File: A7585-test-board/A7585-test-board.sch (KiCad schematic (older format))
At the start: 25 parts, among them J100 Conn_Coaxial_Power, SW201 SW_SPDT, SW302 SW_Push_SPDT, SW303 SW_Push_SPDT, U100 MPM3610, U200 A7585D, U300 Pico

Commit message: Minor schematic changes. Layout V1
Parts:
- added H1, H2, H3, H4: MountingHole, MountingHole:MountingHole_3.2mm_M3, symbol Mechanical:MountingHole
- added J2, J3: Conn_01x20, Connector_PinHeader_2.54mm:PinHeader_1x20_P2.54mm_Vertical, symbol Connector_Generic:Conn_01x20
- added J4: Conn_Coaxial_Power, Connector:Banana_Jack_1Pin, symbol Connector:Conn_Coaxial_Power
- C202, C204: footprint (none) -> Capacitor_SMD:C_1206_3216Metric
- D101, D201, D202, D300, D301: footprint (none) -> LED_THT:LED_D4.0mm
- J1: renamed from J?; footprint (none) -> A7585-test-board:Connector_Strip
- J100: footprint (none) -> Connector_BarrelJack:BarrelJack_Horizontal
- JP201, JP202, JP3: footprint (none) -> Connector_PinHeader_2.54mm:PinHeader_1x02_P2.54mm_Vertical
- R101, R201, R202, R203, R204, R301: footprint (none) -> Resistor_SMD:R_1206_3216Metric
- RV301: footprint (none) -> A7585-test-board:Potentiometer_Piher_T-16H_Single_Horizontal
- SW201: footprint (none) -> A7585-test-board:SW_DIP_SPSTx01_Slide_9.78x4.72mm_W7.62mm_P2.54mm
- SW302, SW303: footprint (none) -> A7585-test-board:PUSH_BUTTON
- U100: footprint (none) -> A7585-test-board:MPM3610
- U200: footprint (none) -> A7585-test-board:A7585D_Board
- U300: footprint RPi_Pico:RPi_Pico_SMD_TH -> A7585-test-board:RPi_Pico_SMD_TH
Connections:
- net labels removed: Vdrive

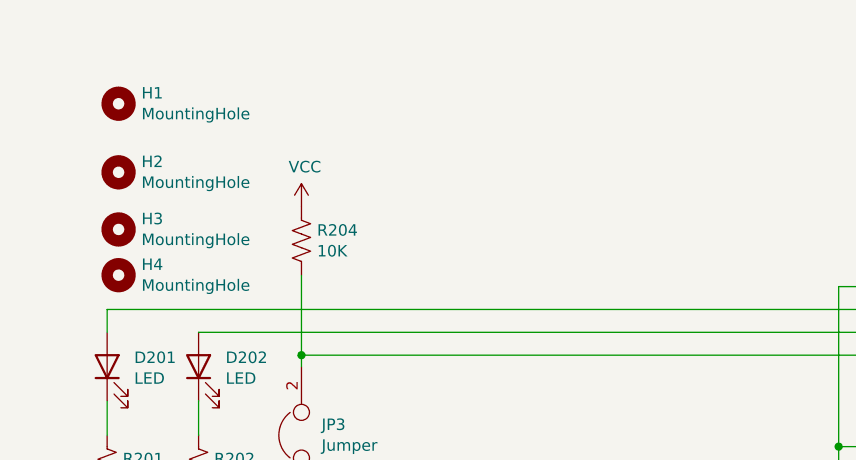
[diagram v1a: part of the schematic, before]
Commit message: Grounded mounting holes. Fixed power plane
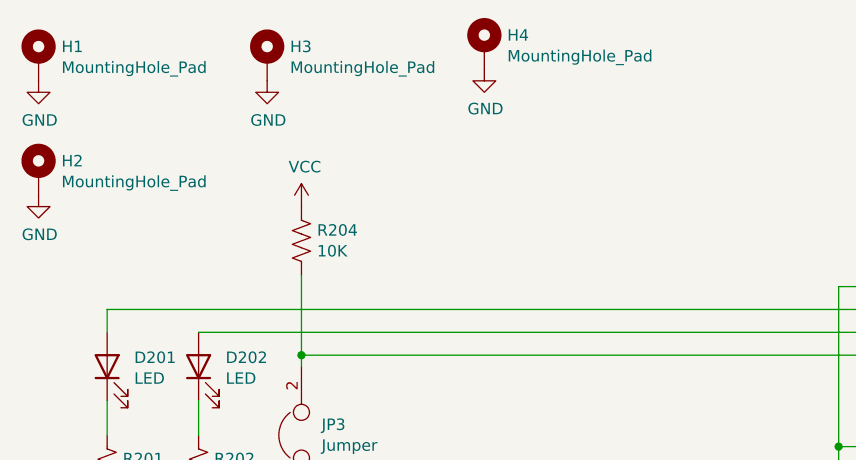
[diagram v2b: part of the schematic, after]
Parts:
- removed H1, H2, H3, H4: MountingHole, MountingHole:MountingHole_3.2mm_M3, symbol Mechanical:MountingHole
- added H1, H2, H3, H4: MountingHole_Pad, MountingHole:MountingHole_3.2mm_M3_Pad, symbol Mechanical:MountingHole_Pad
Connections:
- net GND: now also H1.1, H2.1, H3.1, H4.1
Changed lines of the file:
@@
 	950  1950 950  1850
-$Comp
-L Device:Jumper JP3
-U 1 1 60BA667A
-P 1800 2400
-F 0 "JP3" V 1846 2312 50  0000 R CNN
-F 1 "Jumper" V 1755 2312 50  0000 R CNN
-F 2 "Connector_PinHeader_2.54mm:PinHeader_1x02_P2.54mm_Vertical" H 1800 2400 50  0001 C CNN
-F 3 "~" H 1800 2400 50  0001 C CNN
-	1    1800 2400
-	0    -1   -1   0
-$EndComp
 $Comp
 L Device:R_US R204
@@
 F 3 "~" H 1800 1550 50  0001 C CNN
 	1    1800 1550
-	1    0    0    -1
-$EndComp
-$Comp
-L power:GND #PWR0107
-U 1 1 60BAB54E
-P 1800 2700
-F 0 "#PWR0107" H 1800 2450 50  0001 C CNN
-F 1 "GND" H 1805 2527 50  0000 C CNN
-F 2 "" H 1800 2700 50  0001 C CNN
-F 3 "" H 1800 2700 50  0001 C CNN
-	1    1800 2700
 	1    0    0    -1
 $EndComp
@@
 Text Notes 4250 6150 0    50   ~ 0
 I2C bus 1
-$Comp
-L Mechanical:MountingHole H1
-U 1 1 61100308
-P 1000 950
-F 0 "H1" H 1100 996 50  0000 L CNN
-F 1 "MountingHole" H 1100 905 50  0000 L CNN
-F 2 "MountingHole:MountingHole_3.2mm_M3" H 1000 950 50  0001 C CNN
-F 3 "~" H 1000 950 50  0001 C CNN
-	1    1000 950
-	1    0    0    -1
-$EndComp
-$Comp
-L Mechanical:MountingHole H2
-U 1 1 6110B90D
-P 1000 1250
-F 0 "H2" H 1100 1296 50  0000 L CNN
-F 1 "MountingHole" H 1100 1205 50  0000 L CNN
-F 2 "MountingHole:MountingHole_3.2mm_M3" H 1000 1250 50  0001 C CNN
-F 3 "~" H 1000 1250 50  0001 C CNN
-	1    1000 1250
-	1    0    0    -1
-$EndComp
-$Comp
-L Mechanical:MountingHole H3
-U 1 1 6110BFC1
-P 1000 1500
-F 0 "H3" H 1100 1546 50  0000 L CNN
-F 1 "MountingHole" H 1100 1455 50  0000 L CNN
-F 2 "MountingHole:MountingHole_3.2mm_M3" H 1000 1500 50  0001 C CNN
-F 3 "~" H 1000 1500 50  0001 C CNN
-	1    1000 1500
-	1    0    0    -1
-$EndComp
-$Comp
-L Mechanical:MountingHole H4
-U 1 1 6110C5E9
-P 1000 1700
-F 0 "H4" H 1100 1746 50  0000 L CNN
-F 1 "MountingHole" H 1100 1655 50  0000 L CNN
-F 2 "MountingHole:MountingHole_3.2mm_M3" H 1000 1700 50  0001 C CNN
-F 3 "~" H 1000 1700 50  0001 C CNN
-	1    1000 1700
-	1    0    0    -1
-$EndComp
 Wire Wire Line
 	4150 4850 4600 4850
@@
 	0    -1   1    0
 $EndComp
+$Comp
+L Mechanical:MountingHole_Pad H1
+U 1 1 610A1B28
+P 650 750
+F 0 "H1" H 750 799 50  0000 L CNN
+F 1 "MountingHole_Pad" H 750 708 50  0000 L CNN
+F 2 "MountingHole:MountingHole_3.2mm_M3_Pad" H 650 750 50  0001 C CNN
+F 3 "~" H 650 750 50  0001 C CNN
+	1    650  750
+	1    0    0    -1
+$EndComp
+$Comp
+L Mechanical:MountingHole_Pad H4
+U 1 1 610A2491
+P 2600 700
+F 0 "H4" H 2700 749 50  0000 L CNN
+F 1 "MountingHole_Pad" H 2700 658 50  0000 L CNN
+F 2 "MountingHole:MountingHole_3.2mm_M3_Pad" H 2600 700 50  0001 C CNN
+F 3 "~" H 2600 700 50  0001 C CNN
+	1    2600 700
+	1    0    0    -1
+$EndComp
+$Comp
+L Mechanical:MountingHole_Pad H2
+U 1 1 610A27A1
+P 650 1250
+F 0 "H2" H 750 1299 50  0000 L CNN
+F 1 "MountingHole_Pad" H 750 1208 50  0000 L CNN
+F 2 "MountingHole:MountingHole_3.2mm_M3_Pad" H 650 1250 50  0001 C CNN
+F 3 "~" H 650 1250 50  0001 C CNN
+	1    650  1250
+	1    0    0    -1
+$EndComp
+$Comp
+L Mechanical:MountingHole_Pad H3
+U 1 1 610A333E
+P 1650 750
+F 0 "H3" H 1750 799 50  0000 L CNN
+F 1 "MountingHole_Pad" H 1750 708 50  0000 L CNN
+F 2 "MountingHole:MountingHole_3.2mm_M3_Pad" H 1650 750 50  0001 C CNN
+F 3 "~" H 1650 750 50  0001 C CNN
+	1    1650 750
+	1    0    0    -1
+$EndComp
+$Comp
+L power:GND #PWR0107
+U 1 1 60BAB54E
+P 1800 2700
+F 0 "#PWR0107" H 1800 2450 50  0001 C CNN
+F 1 "GND" H 1805 2527 50  0000 C CNN
+F 2 "" H 1800 2700 50  0001 C CNN
+F 3 "" H 1800 2700 50  0001 C CNN
+	1    1800 2700
+	1    0    0    -1
+$EndComp
+$Comp
+L Device:Jumper JP3
+U 1 1 60BA667A
+P 1800 2400
+F 0 "JP3" V 1846 2312 50  0000 R CNN
+F 1 "Jumper" V 1755 2312 50  0000 R CNN
+F 2 "Connector_PinHeader_2.54mm:PinHeader_1x02_P2.54mm_Vertical" H 1800 2400 50  0001 C CNN
+F 3 "~" H 1800 2400 50  0001 C CNN
+	1    1800 2400
+	0    -1   -1   0
+$EndComp
+$Comp
+L power:GND #PWR03
+U 1 1 610A737A
+P 1650 850
+F 0 "#PWR03" H 1650 600 50  0001 C CNN
+F 1 "GND" H 1655 677 50  0000 C CNN
+F 2 "" H 1650 850 50  0001 C CNN
+F 3 "" H 1650 850 50  0001 C CNN
+	1    1650 850
+	1    0    0    -1
+$EndComp
+$Comp
+L power:GND #PWR04
+U 1 1 610A79D5
+P 2600 800
+F 0 "#PWR04" H 2600 550 50  0001 C CNN
+F 1 "GND" H 2605 627 50  0000 C CNN
+F 2 "" H 2600 800 50  0001 C CNN
+F 3 "" H 2600 800 50  0001 C CNN
+	1    2600 800
+	1    0    0    -1
+$EndComp
+$Comp
+L power:GND #PWR02
+U 1 1 610A7D20
+P 650 1350
+F 0 "#PWR02" H 650 1100 50  0001 C CNN
+F 1 "GND" H 655 1177 50  0000 C CNN
+F 2 "" H 650 1350 50  0001 C CNN
+F 3 "" H 650 1350 50  0001 C CNN
+	1    650  1350
+	1    0    0    -1
+$EndComp
+$Comp
+L power:GND #PWR01
+U 1 1 610A8025
+P 650 850
+F 0 "#PWR01" H 650 600 50  0001 C CNN
+F 1 "GND" H 655 677 50  0000 C CNN
+F 2 "" H 650 850 50  0001 C CNN
+F 3 "" H 650 850 50  0001 C CNN
+	1    650  850
+	1    0    0    -1
+$EndComp
 $EndSCHEMATC

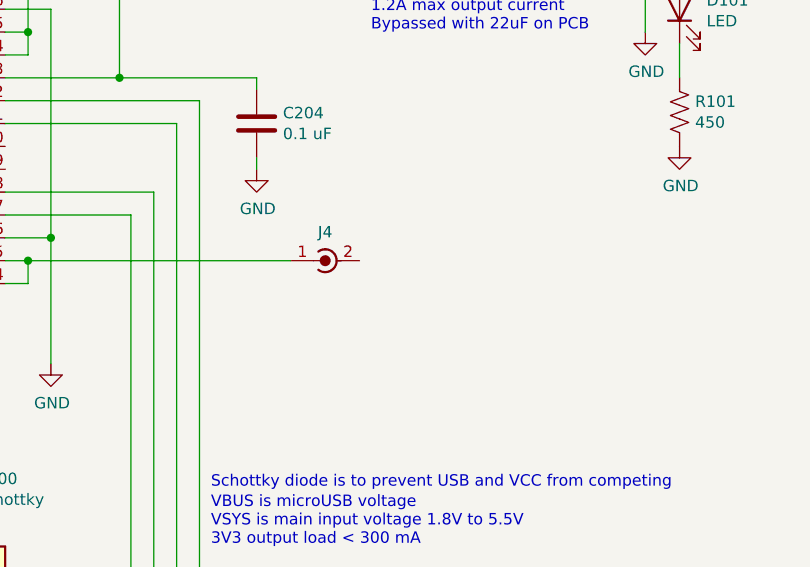
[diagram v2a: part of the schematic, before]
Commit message: New Banana Jacks
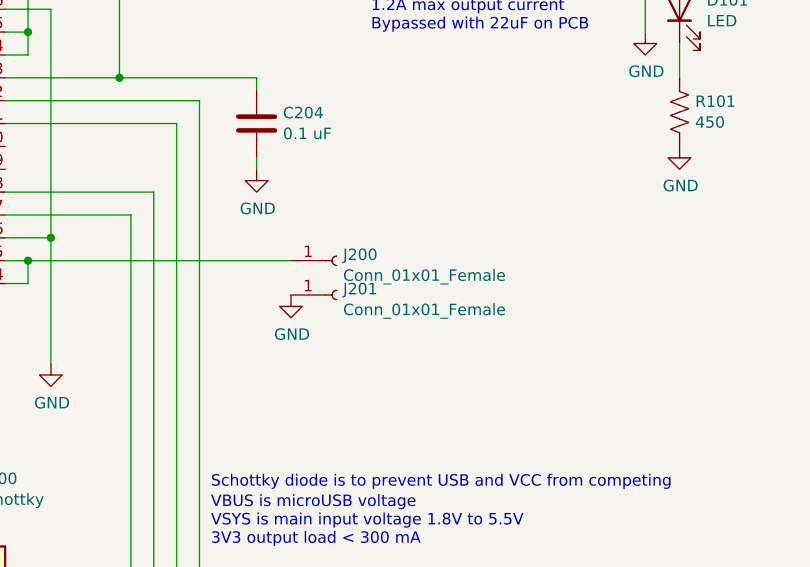
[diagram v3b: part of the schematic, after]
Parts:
- removed J4: Conn_Coaxial_Power, Connector:Banana_Jack_1Pin, symbol Connector:Conn_Coaxial_Power
- added J200, J201: Conn_01x01_Female, A7585-test-board:SMA_Molex_73251-2200_Horizontal, symbol Connector:Conn_01x01_Female
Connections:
- net GND: now also J201.1 (Pin_1)
- net at U200.14 (HV_OUT), U200.15 (HV_OUT): now also J200.1 (Pin_1)
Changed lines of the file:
@@
 	6350 2850 7500 2850
-$Comp
-L Connector:Conn_Coaxial_Power J4
-U 1 1 611FF83A
-P 7600 2850
-F 0 "J4" V 7475 2800 50  0000 C CNN
-F 1 "Conn_Coaxial_Power" H 7688 2755 50  0001 L CNN
-F 2 "Connector:Banana_Jack_1Pin" H 7600 2800 50  0001 C CNN
-F 3 "~" H 7600 2800 50  0001 C CNN
-	1    7600 2850
-	0    -1   1    0
-$EndComp
 $Comp
 L Mechanical:MountingHole_Pad H1
@@
 	1    0    0    -1
 $EndComp
+$Comp
+L power:GND #PWR0113
+U 1 1 610EF2A9
+P 7500 3000
+F 0 "#PWR0113" H 7500 2750 50  0001 C CNN
+F 1 "GND" H 7505 2827 50  0000 C CNN
+F 2 "" H 7500 3000 50  0001 C CNN
+F 3 "" H 7500 3000 50  0001 C CNN
+	1    7500 3000
+	1    0    0    -1
+$EndComp
+$Comp
+L Connector:Conn_01x01_Female J200
+U 1 1 6111CAAF
+P 7700 2850
+F 0 "J200" H 7728 2876 50  0000 L CNN
+F 1 "Conn_01x01_Female" H 7728 2785 50  0000 L CNN
+F 2 "A7585-test-board:SMA_Molex_73251-2200_Horizontal" H 7700 2850 50  0001 C CNN
+F 3 "~" H 7700 2850 50  0001 C CNN
+	1    7700 2850
+	1    0    0    -1
+$EndComp
+$Comp
+L Connector:Conn_01x01_Female J201
+U 1 1 6111D07E
+P 7700 3000
+F 0 "J201" H 7728 3026 50  0000 L CNN
+F 1 "Conn_01x01_Female" H 7728 2935 50  0000 L CNN
+F 2 "A7585-test-board:SMA_Molex_73251-2200_Horizontal" H 7700 3000 50  0001 C CNN
+F 3 "~" H 7700 3000 50  0001 C CNN
+	1    7700 3000
+	1    0    0    -1
+$EndComp

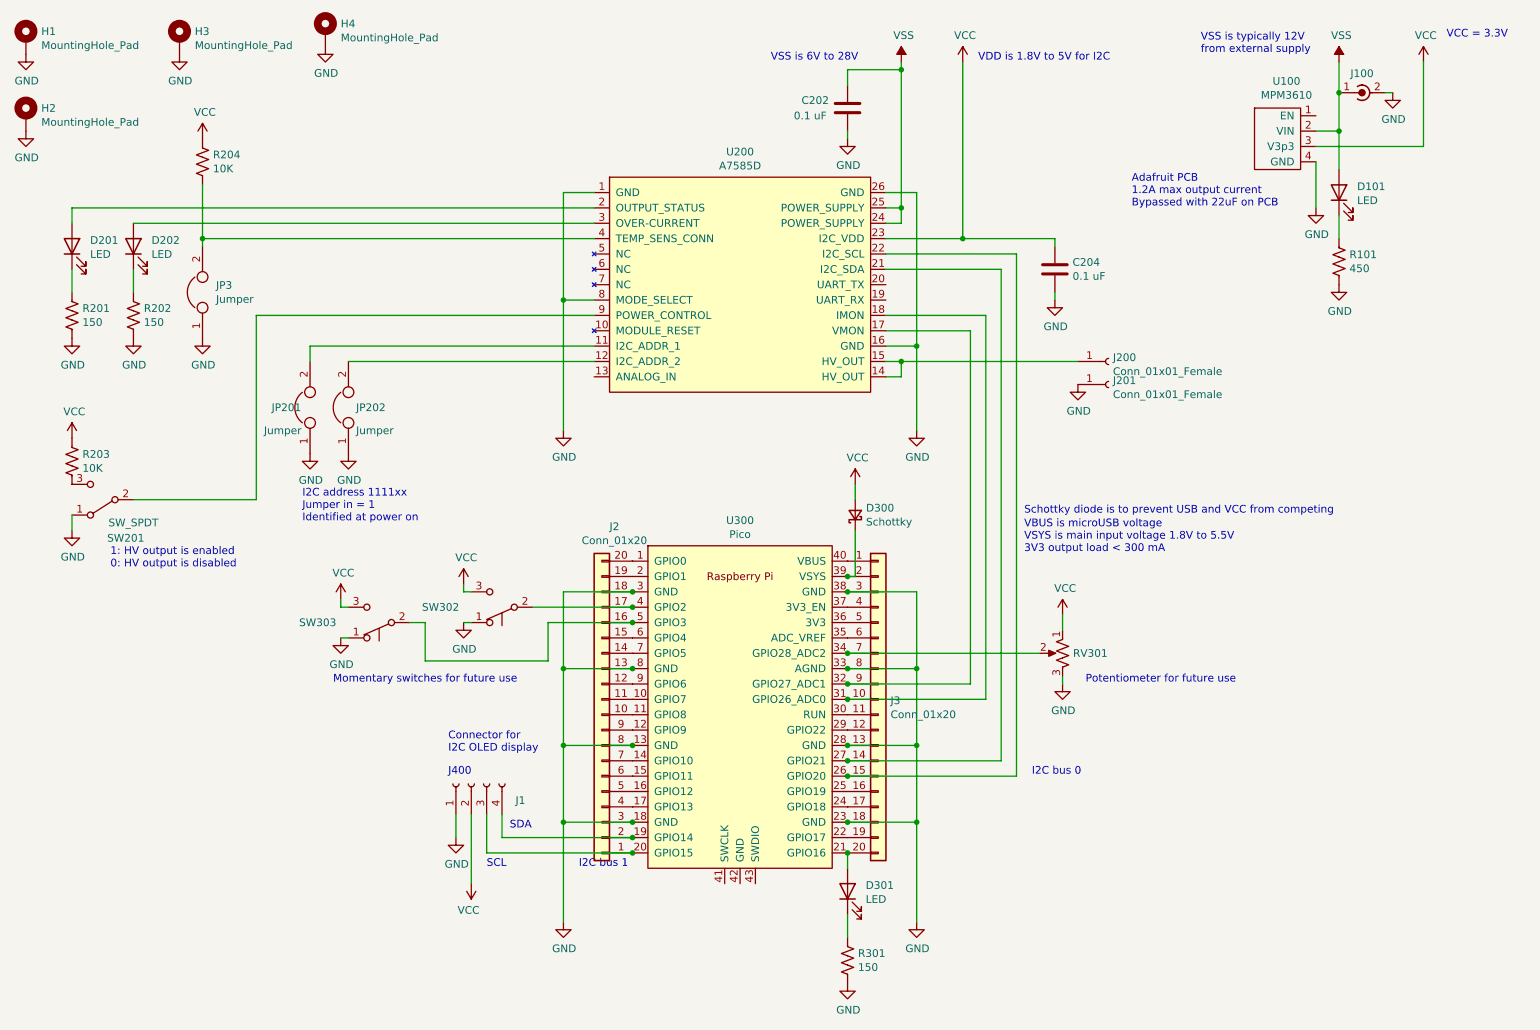
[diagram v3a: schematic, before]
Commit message: New circuit diagram with rotary encoder and precision voltage reference.
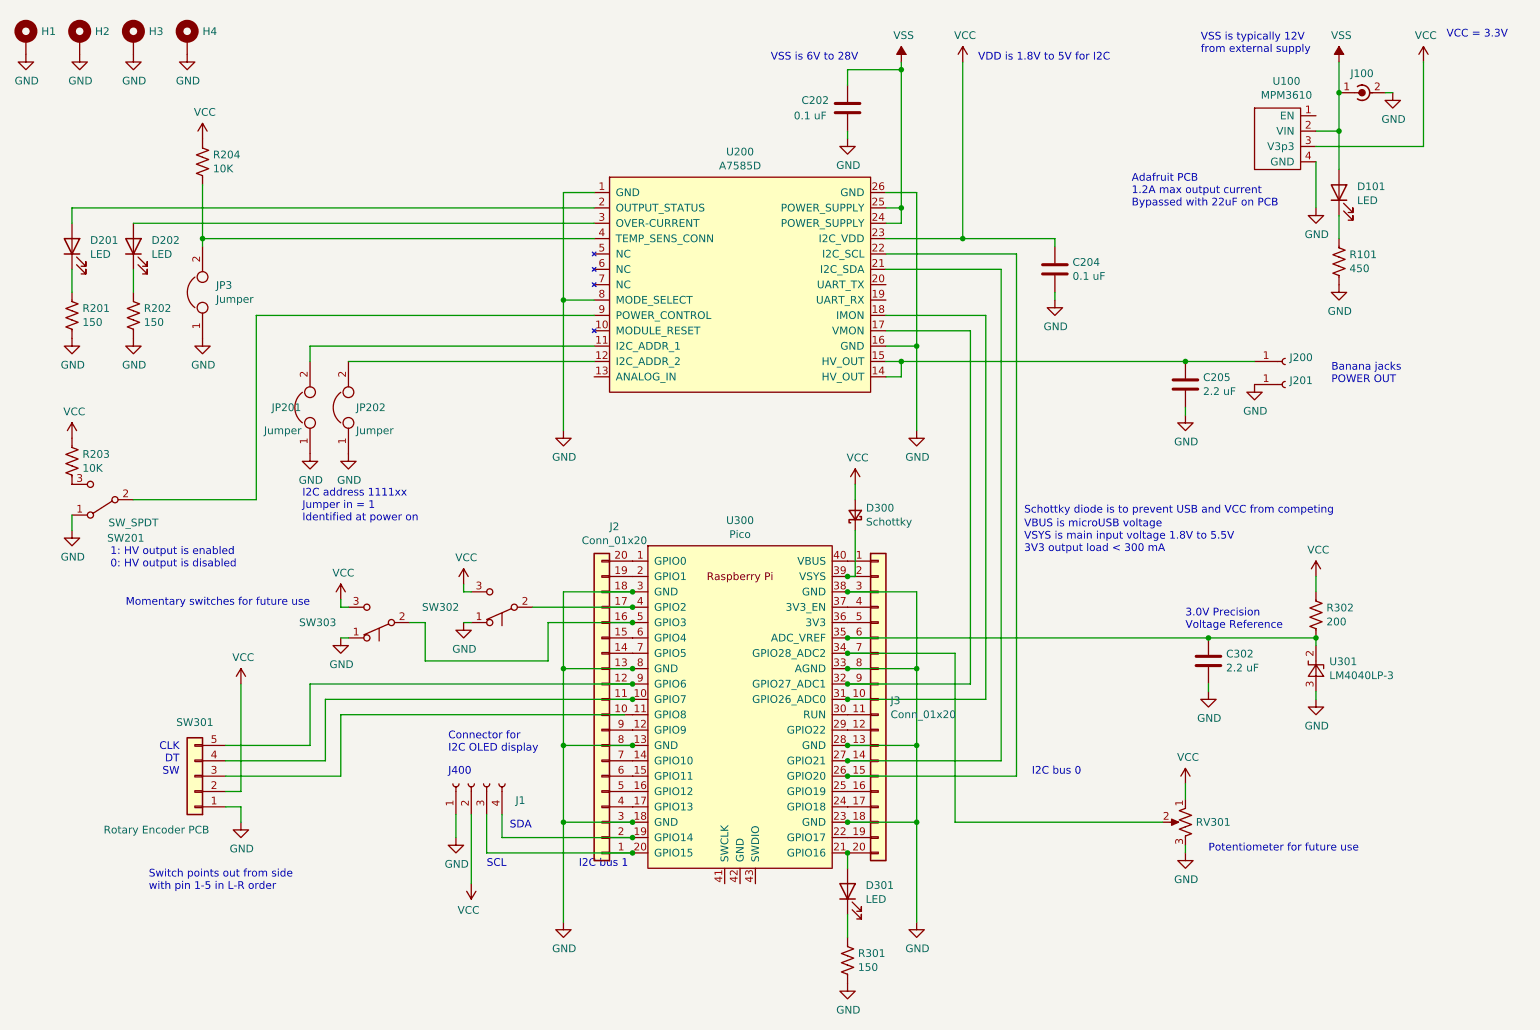
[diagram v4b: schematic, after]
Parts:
- added C205, C302: 2.2 uF, Capacitor_SMD:C_1206_3216Metric, symbol Device:C
- added R302: 200, Resistor_SMD:R_1206_3216Metric, symbol Device:R_US
- added SW301: Rotary Encoder PCB, symbol Connector_Generic:Conn_01x05
- added U301: LM4040LP-3, Package_TO_SOT_THT:TO-92_Inline, symbol Reference_Voltage:LM4040LP-3
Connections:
- net GND: now also C205.2, C302.2, SW301.1 (Pin_1), U301.3 (A)
- net VCC: now also R302.1, SW301.2 (Pin_2)
- net at J200.1 (Pin_1), U200.14 (HV_OUT), U200.15 (HV_OUT): now also C205.1
- net at J2.11 (Pin_11), U300.10 (GPIO7): now also SW301.4 (Pin_4)
- net at J3.6 (Pin_6), U300.35 (ADC_VREF): now also C302.1, R302.2, U301.2 (K)
- net at J2.12 (Pin_12), U300.9 (GPIO6): now also SW301.5 (Pin_5)
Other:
- note added: "3.0V Precision \nVoltage Reference"
- note added: "Banana jacks\nPOWER OUT"
- note added: "CLK\nDT\nSW"
- note added: "Switch points out from side\nwith pin 1-5 in L-R order"
- moved on the sheet: H2, H3, H4, J200, J201, RV301

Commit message: Add files via upload
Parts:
- J200, J201: footprint A7585-test-board:SMA_Molex_73251-2200_Horizontal -> A7585-test-board:Bannana_Jack_2pin
- SW301: footprint (none) -> Connector_PinHeader_2.54mm:PinHeader_1x05_P2.54mm_Vertical
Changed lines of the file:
@@
 F 0 "J200" H 8878 2876 50  0000 L CNN
 F 1 "Conn_01x01_Female" H 8878 2785 50  0001 L CNN
-F 2 "A7585-test-board:SMA_Molex_73251-2200_Horizontal" H 8850 2850 50  0001 C CNN
+F 2 "A7585-test-board:Bannana_Jack_2pin" H 8850 2850 50  0001 C CNN
 F 3 "~" H 8850 2850 50  0001 C CNN
 	1    8850 2850
@@
 F 0 "J201" H 8878 3026 50  0000 L CNN
 F 1 "Conn_01x01_Female" H 8878 2935 50  0001 L CNN
-F 2 "A7585-test-board:SMA_Molex_73251-2200_Horizontal" H 8850 3000 50  0001 C CNN
+F 2 "A7585-test-board:Bannana_Jack_2pin" H 8850 3000 50  0001 C CNN
 F 3 "~" H 8850 3000 50  0001 C CNN
 	1    8850 3000
@@
 F 0 "SW301" H 1750 5200 50  0000 C CNN
 F 1 "Rotary Encoder PCB" H 2000 5900 50  0000 C CNN
-F 2 "" H 1750 5550 50  0001 C CNN
+F 2 "Connector_PinHeader_2.54mm:PinHeader_1x05_P2.54mm_Vertical" H 1750 5550 50  0001 C CNN
 F 3 "~" H 1750 5550 50  0001 C CNN
 	1    1750 5550
@@
 $EndComp
 $Comp
-L power:GND #PWR?
+L power:GND #PWR0133
 U 1 1 61417CFC
 P 2050 5850
-F 0 "#PWR?" H 2050 5600 50  0001 C CNN
+F 0 "#PWR0133" H 2050 5600 50  0001 C CNN
 F 1 "GND" H 2055 5677 50  0000 C CNN
 F 2 "" H 2050 5850 50  0001 C CNN
@@
 $EndComp
 $Comp
-L power:VCC #PWR?
+L power:VCC #PWR0134
 U 1 1 614188AF
 P 2050 4950
-F 0 "#PWR?" H 2050 4800 50  0001 C CNN
+F 0 "#PWR0134" H 2050 4800 50  0001 C CNN
 F 1 "VCC" H 2065 5123 50  0000 C CNN
 F 2 "" H 2050 4950 50  0001 C CNN
@@
 	9050 4650 9050 4700
 $Comp
-L power:GND #PWR?
+L power:GND #PWR0135
 U 1 1 6147B224
 P 9050 5050
-F 0 "#PWR?" H 9050 4800 50  0001 C CNN
+F 0 "#PWR0135" H 9050 4800 50  0001 C CNN
 F 1 "GND" H 9055 4877 50  0000 C CNN
 F 2 "" H 9050 5050 50  0001 C CNN
@@
 $EndComp
 $Comp
-L power:VCC #PWR?
+L power:VCC #PWR0136
 U 1 1 6147BFCC
 P 9050 4250
-F 0 "#PWR?" H 9050 4100 50  0001 C CNN
+F 0 "#PWR0136" H 9050 4100 50  0001 C CNN
 F 1 "VCC" H 9065 4423 50  0000 C CNN
 F 2 "" H 9050 4250 50  0001 C CNN
@@
 $EndComp
 $Comp
-L power:GND #PWR?
+L power:GND #PWR0137
 U 1 1 614D7B19
 P 8200 3200
-F 0 "#PWR?" H 8200 2950 50  0001 C CNN
+F 0 "#PWR0137" H 8200 2950 50  0001 C CNN
 F 1 "GND" H 8205 3027 50  0000 C CNN
 F 2 "" H 8200 3200 50  0001 C CNN
@@
 $EndComp
 $Comp
-L power:GND #PWR?
+L power:GND #PWR0138
 U 1 1 614E540C
 P 8350 5000
-F 0 "#PWR?" H 8350 4750 50  0001 C CNN
+F 0 "#PWR0138" H 8350 4750 50  0001 C CNN
 F 1 "GND" H 8355 4827 50  0000 C CNN
 F 2 "" H 8350 5000 50  0001 C CNN
